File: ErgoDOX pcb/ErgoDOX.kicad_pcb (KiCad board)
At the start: 2 copper layers, 182.8 x 158.9 mm, 75 parts, among them J1 USB, J2 3.5mm, J3 JMP, J4 JMP, SW0:10 SW0:3, SW0:11 SW0:2, SW0:12 SW0:1, SW0:7 SW0:6, SW0:8 SW0:5, SW0:9 SW0:4, SW1:10 SW1:3, SW1:11 SW1:2, SW1:12 SW1:1, SW1:13 SW1:0, SW1:9 SW1:4, SW2:10 SW2:3, SW2:11 SW2:2, SW2:12 SW2:1, SW2:13 SW2:0, SW2:7 SW2:6, SW2:8 SW2:5, SW2:9 SW2:4, SW3:10 SW3:3, SW3:11 SW3:2, SW3:12 SW3:1, SW3:13 SW3:0, SW3:8 SW3:5, SW3:9 SW3:4, SW4:10 SW4:3, SW4:11 SW4:2, SW4:12 SW4:1, SW4:13 SW4:0, SW4:7 SW4:6, SW4:8 SW4:5, SW4:9 SW4:4, SW5:10 SW5:3, SW5:11 SW5:2, SW5:12 SW5:1, SW5:13 SW5:0, SW5:7 SW5:6, SW5:8 SW5:5, SW5:9 SW5:4, U1 TEENSY2.0, U2 MCP23018

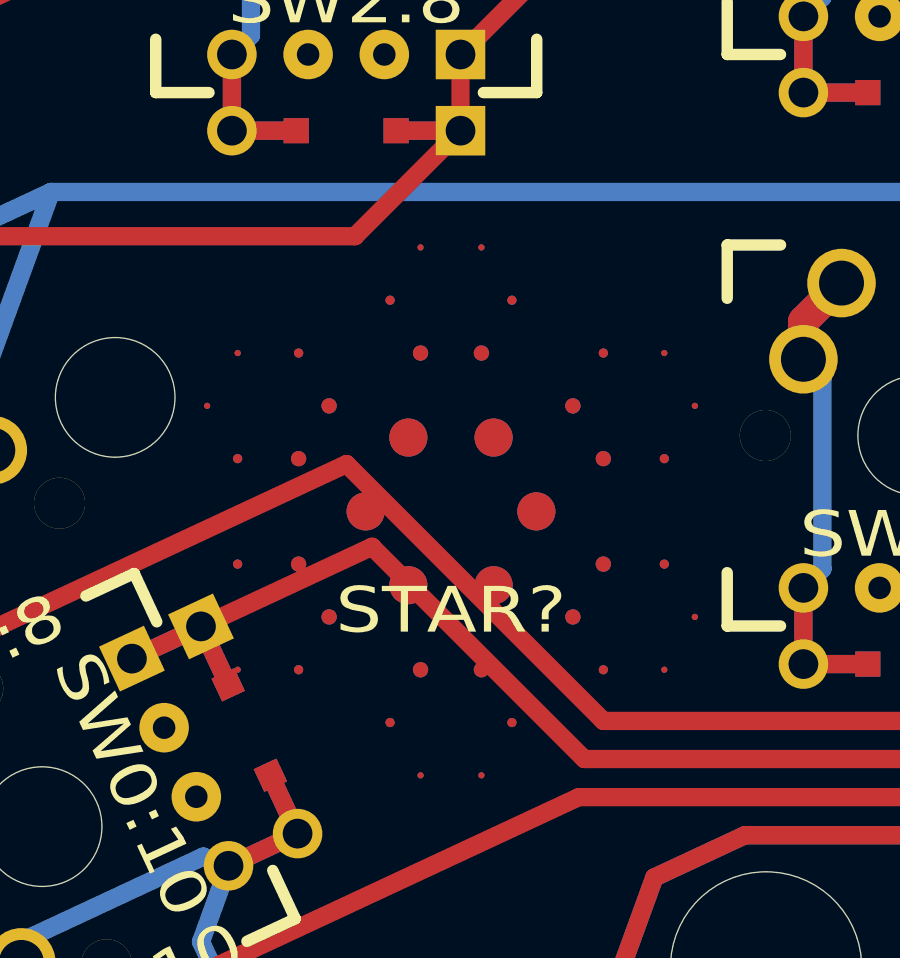
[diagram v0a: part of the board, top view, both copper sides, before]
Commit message: Repl. Star w. OSS HW Logo
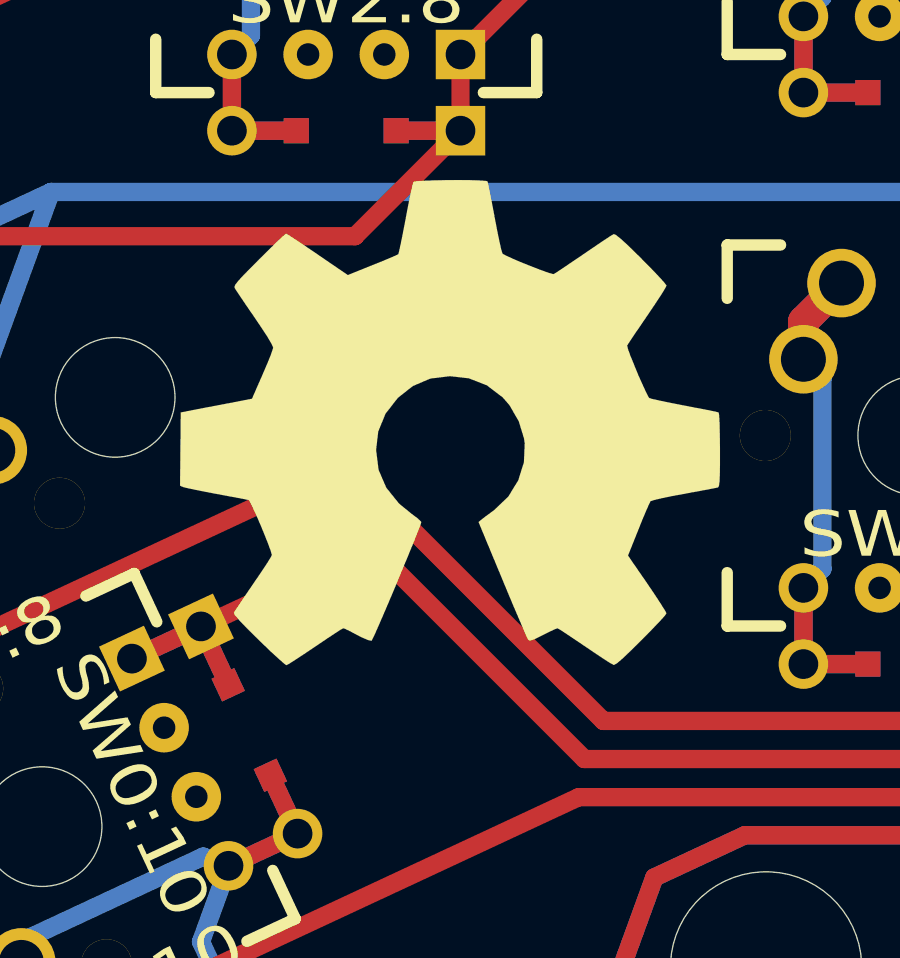
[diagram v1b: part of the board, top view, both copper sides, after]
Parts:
- removed STAR? (x2): STAR, STAR
- added G***: LOGO, OpenSourceHardwareLogo, B.Cu at (94.9, 139.6)
- added G***: LOGO, OpenSourceHardwareLogo, F.Cu at (94.9, 139.6)

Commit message: Add merged drill file, update graphics
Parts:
- removed the G*** at (94.9, 139.6) (x2)
- added G***: LOGO, OpenSourceHardwareLogo, B.Cu at (93.3, 138.5)
- added G***: LOGO, OpenSourceHardwareLogo, F.Cu at (93.3, 138.5)
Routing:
- net GND: track 121.3 -> 120.1 mm
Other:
- board text added: "Revision 2013-11-07 RGB Backlight Edition"
- board text removed: "Revision 2013-10-11 RGB Backlight Edition"
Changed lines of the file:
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@@
 (kicad_pcb (version 3) (host pcbnew "(2013-07-07 BZR 4022)-stable")
   (general
-    (links 512)
-    (no_connects 2)
+    (links 0)
+    (no_connects 3)
     (area 22.890479 28.163519 259.962628 189.542421)
     (thickness 1.6002)
     (drawings 39)
-    (tracks 1331)
+    (tracks 1330)
     (zones 0)
     (modules 75)
@@
     (22 B.Mask user)
     (23 F.Mask user)
-    (24 Dwgs.User user hide)
-    (25 Cmts.User user hide)
-    (26 Eco1.User user hide)
+    (24 Dwgs.User user)
+    (25 Cmts.User user)
+    (26 Eco1.User user)
     (27 Eco2.User user)
-    (28 Edge.Cuts user hide)
+    (28 Edge.Cuts user)
   )
   (setup
@@
       (effects (font (size 0.50038 0.50038) (thickness 0.11938)))
     )
-    (fp_text value L1 (at -0.0254 1.7272 90) (layer F.SilkS) hide
+    (fp_text value L1 (at 2.775 0 180) (layer F.SilkS) hide
       (effects (font (size 0.50038 0.50038) (thickness 0.11938)))
     )
@@
       (effects (font (size 0.5 0.5) (thickness 0.125)) (justify mirror))
     )
-    (fp_text value RGB_LED1 (at 2.794 0 180) (layer B.SilkS)
+    (fp_text value RGB_LED1 (at 2.69 -0.03 180) (layer B.SilkS)
       (effects (font (size 0.5 0.5) (thickness 0.125)) (justify mirror))
     )
@@
     (at 201.93 46.99 270)
     (solder_mask_margin 0.05)
-    (fp_text reference RGB_LED1 (at -2.794 0 360) (layer F.SilkS)
+    (fp_text reference RGB_LED1 (at -2.69 0.03 360) (layer F.SilkS)
       (effects (font (size 0.5 0.5) (thickness 0.125)))
     )
@@
     (at 190.5 55.372 270)
     (descr "SMT capacitor, 1210")
-    (fp_text reference L1 (at 0.028 0.08 360) (layer B.SilkS)
+    (fp_text reference L1 (at -2.772 0 360) (layer B.SilkS)
       (effects (font (size 0.50038 0.50038) (thickness 0.11938)) (justify mirror))
     )
@@
     (at 186.3 55.3 180)
     (descr "SMT capacitor, 1206")
-    (fp_text reference CIN1 (at -0.06 0.04 270) (layer B.SilkS)
+    (fp_text reference CIN1 (at 0 -1.5 180) (layer B.SilkS)
       (effects (font (size 0.50038 0.50038) (thickness 0.11938)) (justify mirror))
     )
@@
     (at 202.5 55.5 270)
     (descr "SMT capacitor, 1206")
-    (fp_text reference COUT1 (at 0.2 1.6 270) (layer B.SilkS)
+    (fp_text reference COUT1 (at 2.9 0 360) (layer B.SilkS)
       (effects (font (size 0.50038 0.50038) (thickness 0.11938)) (justify mirror))
     )
@@
       (effects (font (size 0.50038 0.50038) (thickness 0.11938)))
     )
-    (fp_text value COUT1 (at 0.05 1.65 270) (layer F.SilkS) hide
+    (fp_text value COUT1 (at 2.901 -0.0985 360) (layer F.SilkS) hide
       (effects (font (size 0.50038 0.50038) (thickness 0.11938)))
     )
@@
   )
   (module OpenSourceHardwareLogo (layer Back)
-    (at 94.9 139.6)
-    (fp_text reference G*** (at 0 -9.54532) (layer B.SilkS) hide
+    (at 93.3 138.5 20)
+    (fp_text reference G*** (at 0 -9.54532 20) (layer B.SilkS) hide
       (effects (font (size 0.82042 0.82042) (thickness 0.16256)) (justify mirror))
     )
-    (fp_text value LOGO (at 0 9.54532) (layer B.SilkS) hide
+    (fp_text value LOGO (at 0 9.54532 20) (layer B.SilkS) hide
       (effects (font (size 0.82042 0.82042) (thickness 0.16256)) (justify mirror))
     )
@@
   )
   (module OpenSourceHardwareLogo (layer Front)
-    (at 94.9 139.6)
-    (fp_text reference G*** (at 0 9.54532) (layer F.SilkS) hide
+    (at 93.3 138.5 20)
+    (fp_text reference G*** (at 0 9.54532 20) (layer F.SilkS) hide
       (effects (font (size 0.82042 0.82042) (thickness 0.16256)))
     )
-    (fp_text value LOGO (at 0 -9.54532) (layer F.SilkS) hide
+    (fp_text value LOGO (at 0 -9.54532 20) (layer F.SilkS) hide
       (effects (font (size 0.82042 0.82042) (thickness 0.16256)))
     )
@@
       (xy -5.45592 8.08482)) (layer F.SilkS) (width 0.00254))
   )
-  (gr_text "Revision 2013-10-11 RGB Backlight Edition" (at 178.435 127 90) (layer F.SilkS)
+  (gr_text "Revision 2013-11-07 RGB Backlight Edition" (at 178.435 127 90) (layer F.SilkS)
     (effects (font (size 2.032 1.524) (thickness 0.3048)) (justify left))
   )
@@
     (effects (font (size 1.016 1.27) (thickness 0.2032)))
   )
-  (gr_text ErgoDox (at 113.03 48.895) (layer B.SilkS)
+  (gr_text ErgoDox (at 102.6 48.6) (layer B.SilkS)
     (effects (font (size 8.128 12.192) (thickness 2.032)) (justify mirror))
   )
@@
   (segment (start 194.33032 53.47208) (end 194.33032 52.56968) (width 0.254) (layer Back) (net 27))
   (segment (start 192.278 42.545) (end 189.865 42.545) (width 0.6096) (layer Back) (net 28))
-  (segment (start 192.278 42.545) (end 193.548 42.545) (width 0.6096) (layer Back) (net 28))
   (segment (start 198.26 53.52) (end 198.26 45.24) (width 0.254) (layer Front) (net 28))
   (via (at 198.26 53.52) (size 0.6096) (layers Front Back) (net 28))

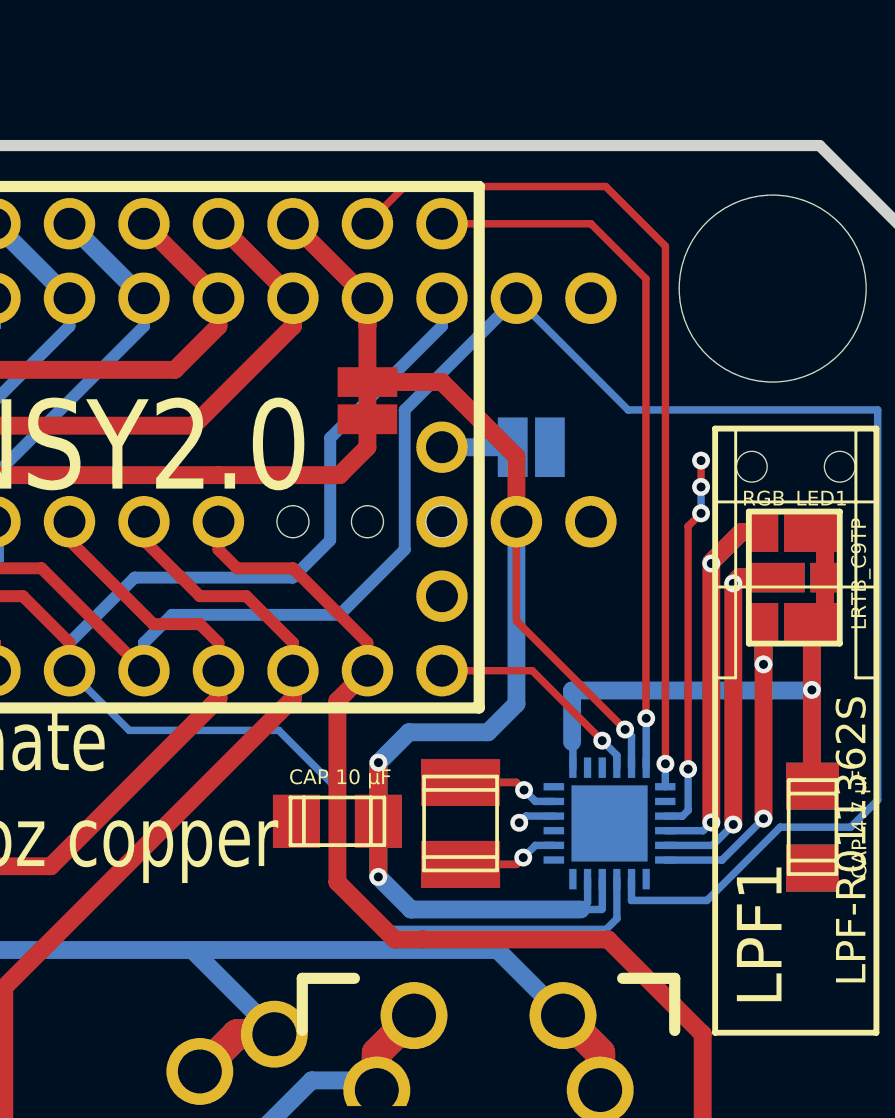
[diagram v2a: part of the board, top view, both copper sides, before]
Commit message: Added I2C debugging Arduino projects
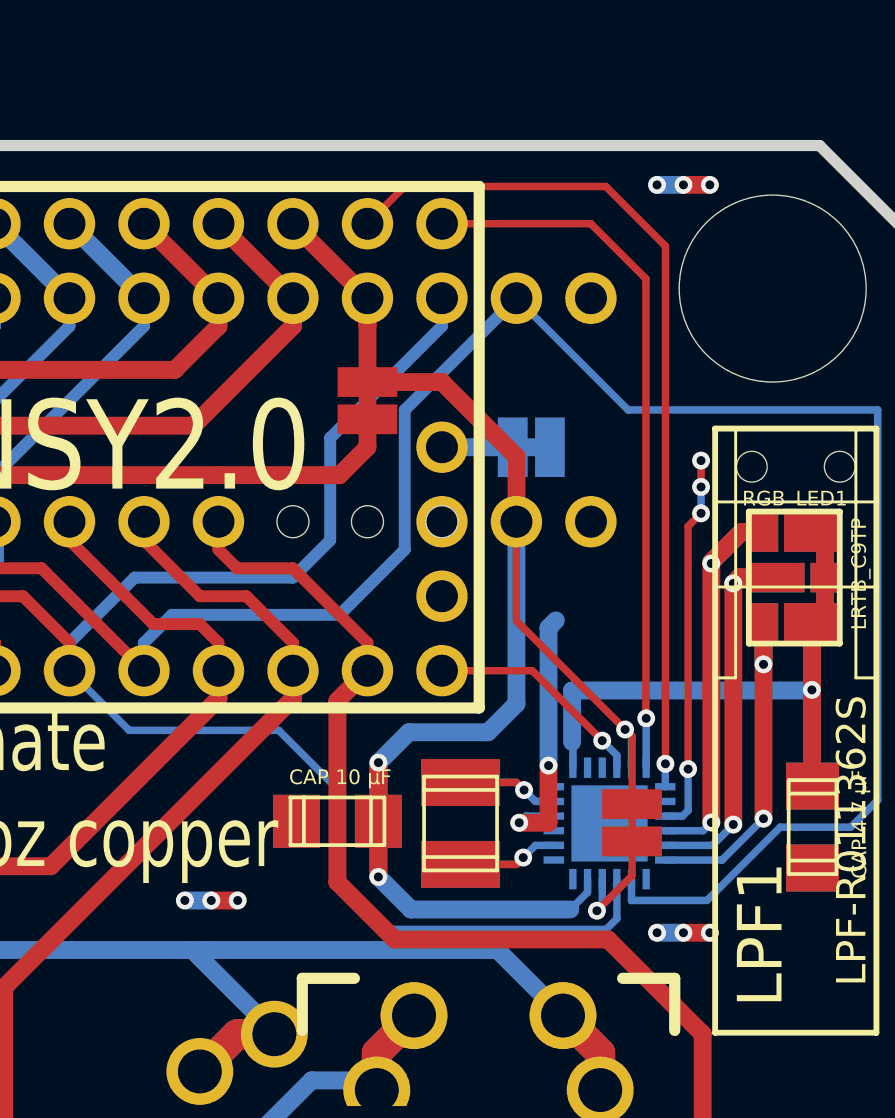
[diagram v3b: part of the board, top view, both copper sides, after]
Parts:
- added GAP: VAL**, GAP, F.Cu at (196.3, 55.4)
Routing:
- net GND: track 120.1 -> 134.7 mm, vias 11 -> 21
- net VCC: track 200.2 -> 206.2 mm, vias 3 -> 4
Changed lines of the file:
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@@
 (kicad_pcb (version 3) (host pcbnew "(2013-07-07 BZR 4022)-stable")
   (general
-    (links 0)
-    (no_connects 3)
+    (links 512)
+    (no_connects 2)
     (area 22.890479 28.163519 259.962628 189.542421)
     (thickness 1.6002)
     (drawings 39)
-    (tracks 1330)
+    (tracks 1356)
     (zones 0)
-    (modules 75)
+    (modules 76)
     (nets 75)
   )
@@
     (18 B.Paste user hide)
     (19 F.Paste user hide)
-    (20 B.SilkS user)
-    (21 F.SilkS user)
-    (22 B.Mask user)
-    (23 F.Mask user)
-    (24 Dwgs.User user)
-    (25 Cmts.User user)
-    (26 Eco1.User user)
-    (27 Eco2.User user)
-    (28 Edge.Cuts user)
+    (20 B.SilkS user hide)
+    (21 F.SilkS user hide)
+    (22 B.Mask user hide)
+    (23 F.Mask user hide)
+    (24 Dwgs.User user hide)
+    (25 Cmts.User user hide)
+    (26 Eco1.User user hide)
+    (27 Eco2.User user hide)
+    (28 Edge.Cuts user hide)
   )
   (setup
-    (last_trace_width 0.3048)
+    (last_trace_width 0.6096)
     (user_trace_width 0.03302)
     (user_trace_width 0.1524)
@@
       (xy -5.45592 8.08482)) (layer F.SilkS) (width 0.00254))
   )
+  (module GAP (layer Front)
+    (at 196.35 55.35)
+    (fp_text reference GAP (at 0 0) (layer F.SilkS) hide
+      (effects (font (size 1.27 1.016) (thickness 0.2032)))
+    )
+    (fp_text value VAL** (at 0 0) (layer F.SilkS) hide
+      (effects (font (size 1.27 1.016) (thickness 0.2032)))
+    )
+    (pad 1 smd rect (at 0 -0.635) (size 2.032 1.016)
+      (layers Front F.Paste F.Mask)
+    )
+    (pad 1 smd rect (at 0 0.635) (size 2.032 1.016)
+      (layers Front F.Paste F.Mask)
+    )
+  )
   (gr_text "Revision 2013-11-07 RGB Backlight Edition" (at 178.435 127 90) (layer F.SilkS)
     (effects (font (size 2.032 1.524) (thickness 0.3048)) (justify left))
@@
   (segment (start 202.93 45.89) (end 202.48 45.44) (width 0.6096) (layer Front) (net 27))
   (segment (start 194.33032 53.47208) (end 194.33032 52.56968) (width 0.254) (layer Back) (net 27))
+  (via (at 197.2 59.1) (size 0.6096) (layers Front Back) (net 28))
+  (via (at 199 59.1) (size 0.6096) (layers Front Back) (net 28))
+  (segment (start 199 59.1) (end 198.1 59.1) (width 0.6096) (layer Front) (net 28))
+  (via (at 198.1 59.1) (size 0.6096) (layers Front Back) (net 28))
+  (segment (start 198.1 59.1) (end 197.2 59.1) (width 0.6096) (layer Back) (net 28))
+  (via (at 181.1 58) (size 0.6096) (layers Front Back) (net 28))
+  (via (at 182.9 58) (size 0.6096) (layers Front Back) (net 28))
+  (segment (start 182.9 58) (end 182 58) (width 0.6096) (layer Front) (net 28))
+  (via (at 182 58) (size 0.6096) (layers Front Back) (net 28))
+  (segment (start 182 58) (end 181.1 58) (width 0.6096) (layer Back) (net 28))
+  (via (at 197.2 33.6) (size 0.6096) (layers Front Back) (net 28))
+  (via (at 199 33.6) (size 0.6096) (layers Front Back) (net 28))
+  (segment (start 199 33.6) (end 198.1 33.6) (width 0.6096) (layer Front) (net 28))
+  (via (at 198.1 33.6) (size 0.6096) (layers Front Back) (net 28))
+  (segment (start 198.1 33.6) (end 197.2 33.6) (width 0.6096) (layer Back) (net 28))
+  (segment (start 192.278 42.545) (end 193.548 42.545) (width 0.6096) (layer Back) (net 28))
+  (via (at 192.5 55.35) (size 0.6096) (layers Front Back) (net 28))
+  (segment (start 192.72692 55.12308) (end 192.5 55.35) (width 0.254) (layer Back) (net 28))
+  (segment (start 192.72692 55.12308) (end 193.68008 55.12308) (width 0.254) (layer Back) (net 28))
+  (segment (start 193.5 55.35) (end 192.5 55.35) (width 0.6096) (layer Front) (net 28))
+  (segment (start 193.5 53.4) (end 193.5 55.35) (width 0.6096) (layer Front) (net 28))
+  (via (at 193.5 53.4) (size 0.6096) (layers Front Back) (net 28))
+  (segment (start 193.5 48.7) (end 193.5 53.4) (width 0.6096) (layer Back) (net 28))
+  (segment (start 193.75 48.45) (end 193.5 48.7) (width 0.6096) (layer Back) (net 28))
   (segment (start 192.278 42.545) (end 189.865 42.545) (width 0.6096) (layer Back) (net 28))
   (segment (start 198.26 53.52) (end 198.26 45.24) (width 0.254) (layer Front) (net 28))
@@
   (via (at 198.7 44.8) (size 0.6096) (layers Front Back) (net 28))
   (segment (start 198.26 45.24) (end 198.7 44.8) (width 0.254) (layer Front) (net 28))
-  (via (at 192.5 55.35) (size 0.6096) (layers Front Back) (net 28))
-  (segment (start 192.72692 55.12308) (end 192.5 55.35) (width 0.254) (layer Back) (net 28))
-  (segment (start 193.68008 55.12308) (end 192.72692 55.12308) (width 0.254) (layer Back) (net 28))
   (segment (start 162.56 143.20266) (end 161.925 143.83766) (width 0.03302) (layer Back) (net 28))
   (segment (start 161.925 149.5425) (end 160.655 150.8125) (width 0.03302) (layer Back) (net 28))
@@
   (segment (start 71.74738 170.13428) (end 72.59066 170.44162) (width 0.6096) (layer Back) (net 73))
   (segment (start 69.33184 164.95522) (end 71.74738 170.13428) (width 0.6096) (layer Back) (net 73))
-  (segment (start 194.8307 57.27192) (end 194.8307 58.0766) (width 0.254) (layer Back) (net 74))
-  (segment (start 194.8307 58.0766) (end 194.6 58.3073) (width 0.254) (layer Back) (net 74))
+  (segment (start 196.35 55.985) (end 196.35 54.715) (width 0.254) (layer Front) (net 74))
+  (segment (start 196.35 54.715) (end 196.35 52.41) (width 0.254) (layer Front) (net 74))
+  (segment (start 196.35 52.41) (end 196.11 52.17) (width 0.254) (layer Front) (net 74))
+  (segment (start 195.33108 57.27192) (end 195.33108 58.16892) (width 0.254) (layer Back) (net 74))
+  (segment (start 196.35 57.15) (end 196.35 55.985) (width 0.254) (layer Front) (net 74))
+  (segment (start 195.15 58.35) (end 196.35 57.15) (width 0.254) (layer Front) (net 74))
+  (via (at 195.15 58.35) (size 0.6096) (layers Front Back) (net 74))
+  (segment (start 195.33108 58.16892) (end 195.15 58.35) (width 0.254) (layer Back) (net 74))
+  (segment (start 194.8307 57.27192) (end 194.8307 57.7193) (width 0.254) (layer Back) (net 74))
+  (segment (start 194.8307 57.7193) (end 194.2427 58.3073) (width 0.254) (layer Back) (net 74))
   (segment (start 187.697 57.197) (end 188.8073 58.3073) (width 0.6096) (layer Back) (net 74))
-  (segment (start 188.8073 58.3073) (end 194.6 58.3073) (width 0.6096) (layer Back) (net 74))
+  (segment (start 188.8073 58.3073) (end 194.2427 58.3073) (width 0.6096) (layer Back) (net 74))
   (segment (start 187.697 57.197) (end 187.697 55.3) (width 0.6096) (layer Back) (net 74))
   (segment (start 187.697 55.3) (end 187.7 55.297) (width 0.6096) (layer Back) (net 74))
@@
   (segment (start 196.3293 52.3893) (end 196.11 52.17) (width 0.254) (layer Back) (net 74))
   (via (at 196.11 52.17) (size 0.6096) (layers Front Back) (net 74))
-  (segment (start 195.33108 57.27192) (end 195.33108 58.28792) (width 0.254) (layer Back) (net 74))
-  (segment (start 195.3117 58.3073) (end 194.6 58.3073) (width 0.254) (layer Back) (net 74))
-  (segment (start 195.33108 58.28792) (end 195.3117 58.3073) (width 0.254) (layer Back) (net 74))
   (segment (start 192.405 48.465) (end 192.405 45.085) (width 0.254) (layer Front) (net 74))
   (segment (start 196.11 52.17) (end 192.405 48.465) (width 0.254) (layer Front) (net 74))
